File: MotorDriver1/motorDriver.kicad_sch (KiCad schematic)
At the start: 23 parts, among them Q1 IRLZ44NSTRLPBF, Q2 IRLZ44NSTRLPBF, Q3 IRLZ44NSTRLPBF, Q4 IRLZ44NSTRLPBF

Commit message: Exported final JLCPCB files
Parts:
- removed D1, D2, D3, D4: Power_D, Diode_SMD:D_0201_0603Metric, symbol Diode:1N4001
- added D1, D2, D3, D4: SM5819L2-TP, footprintLib:SDO_SM5819L2-TP_MCE, symbol pcb:SM5819L2-TP
- R1, R2, R5, R6: value 10000 -> 10k
- R3, R4, R7, R8: footprint Resistor_SMD:R_0402_1005Metric -> Resistor_SMD:R_1206_3216Metric
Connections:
- net 5V: now also C1.1 (+), C2.1 (+), D1.1 (K), D2.1 (K), D3.1 (K), D4.1 (K); no longer C1.2 (-), C2.2 (-)
- net GND: now also C1.2 (-), C2.2 (-); no longer C1.1 (+), C2.1 (+)
- net Motor1-: now also D1.2 (A)
- net Motor2-: now also D2.2 (A)
- net Motor3-: now also D3.2 (A)
- net Motor4-: now also D4.2 (A)
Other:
- moved on the sheet: C1, C2

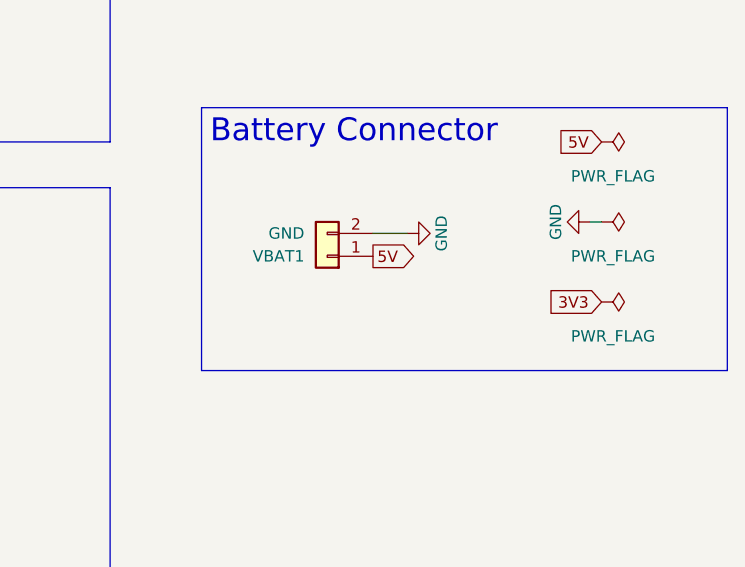
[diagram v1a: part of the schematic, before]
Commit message: Added battery fuse
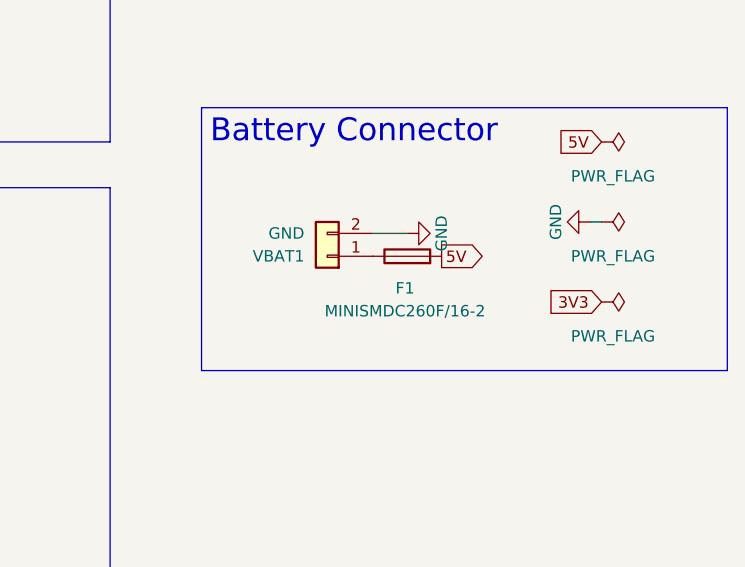
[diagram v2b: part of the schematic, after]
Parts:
- added F1: MINISMDC260F/16-2, Fuse:Fuse_1812_4532Metric, symbol Device:Fuse
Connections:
- net 5V: now also F1.2; no longer VBAT1.1 (Pin_1)
- new net: F1.1, VBAT1.1 (Pin_1)
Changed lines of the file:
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@@
 	)
 	(global_label "5V"
-		(shape input)
-		(at 135.89 29.21 0)
+		(shape output)
+		(at 200.66 106.68 0)
 		(fields_autoplaced yes)
 		(effects
@@
 		)
 		(property "Intersheetrefs" "${INTERSHEET_REFS}"
-			(at 141.1733 29.21 0)
+			(at 205.9433 106.68 0)
 			(effects
 				(font
@@
 	)
 	(global_label "5V"
-		(shape output)
-		(at 193.04 106.68 0)
+		(shape input)
+		(at 135.89 29.21 0)
 		(fields_autoplaced yes)
 		(effects
@@
 		)
 		(property "Intersheetrefs" "${INTERSHEET_REFS}"
-			(at 198.3233 106.68 0)
+			(at 141.1733 29.21 0)
 			(effects
 				(font
@@
 					(unit 1)
 				)
+			)
+		)
+	)
+	(symbol
+		(lib_id "Device:Fuse")
+		(at 196.85 106.68 90)
+		(unit 1)
+		(exclude_from_sim no)
+		(in_bom yes)
+		(on_board yes)
+		(dnp no)
+		(property "Reference" "F1"
+			(at 196.596 110.236 90)
+			(effects
+				(font
+					(size 1.27 1.27)
+				)
+			)
+		)
+		(property "Value" "MINISMDC260F/16-2"
+			(at 196.596 112.776 90)
+			(effects
+				(font
+					(size 1.27 1.27)
+				)
+			)
+		)
+		(property "Footprint" "Fuse:Fuse_1812_4532Metric"
+			(at 196.85 108.458 90)
+			(effects
+				(font
+					(size 1.27 1.27)
+				)
+				(hide yes)
+			)
+		)
+		(property "Datasheet" "~"
+			(at 196.85 106.68 0)
+			(effects
+				(font
+					(size 1.27 1.27)
+				)
+				(hide yes)
+			)
+		)
+		(property "Description" "Fuse"
+			(at 196.85 106.68 0)
+			(effects
+				(font
+					(size 1.27 1.27)
+				)
+				(hide yes)
+			)
+		)
+		(pin "2"
+		)
+		(pin "1"
+		)
+		(instances
+			(project ""
+				(path "/79cc9cfe-04d6-4d00-aa84-feae66cf8c45/bb18fbb4-ec68-4ac2-b714-52f61fe72a01"
+					(reference "F1")
+					(unit 1)
+				)
